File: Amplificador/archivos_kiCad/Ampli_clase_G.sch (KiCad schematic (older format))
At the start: 109 parts, among them J1 Conn_IN, J2 LOAD_CONN, J3 SUPPLY_CONN, Q1 BC856, Q10 BC846, Q11 2SC4793, Q14 2SC4793, Q15 2SA1837, Q16 2SC4793, Q17 2SA1837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

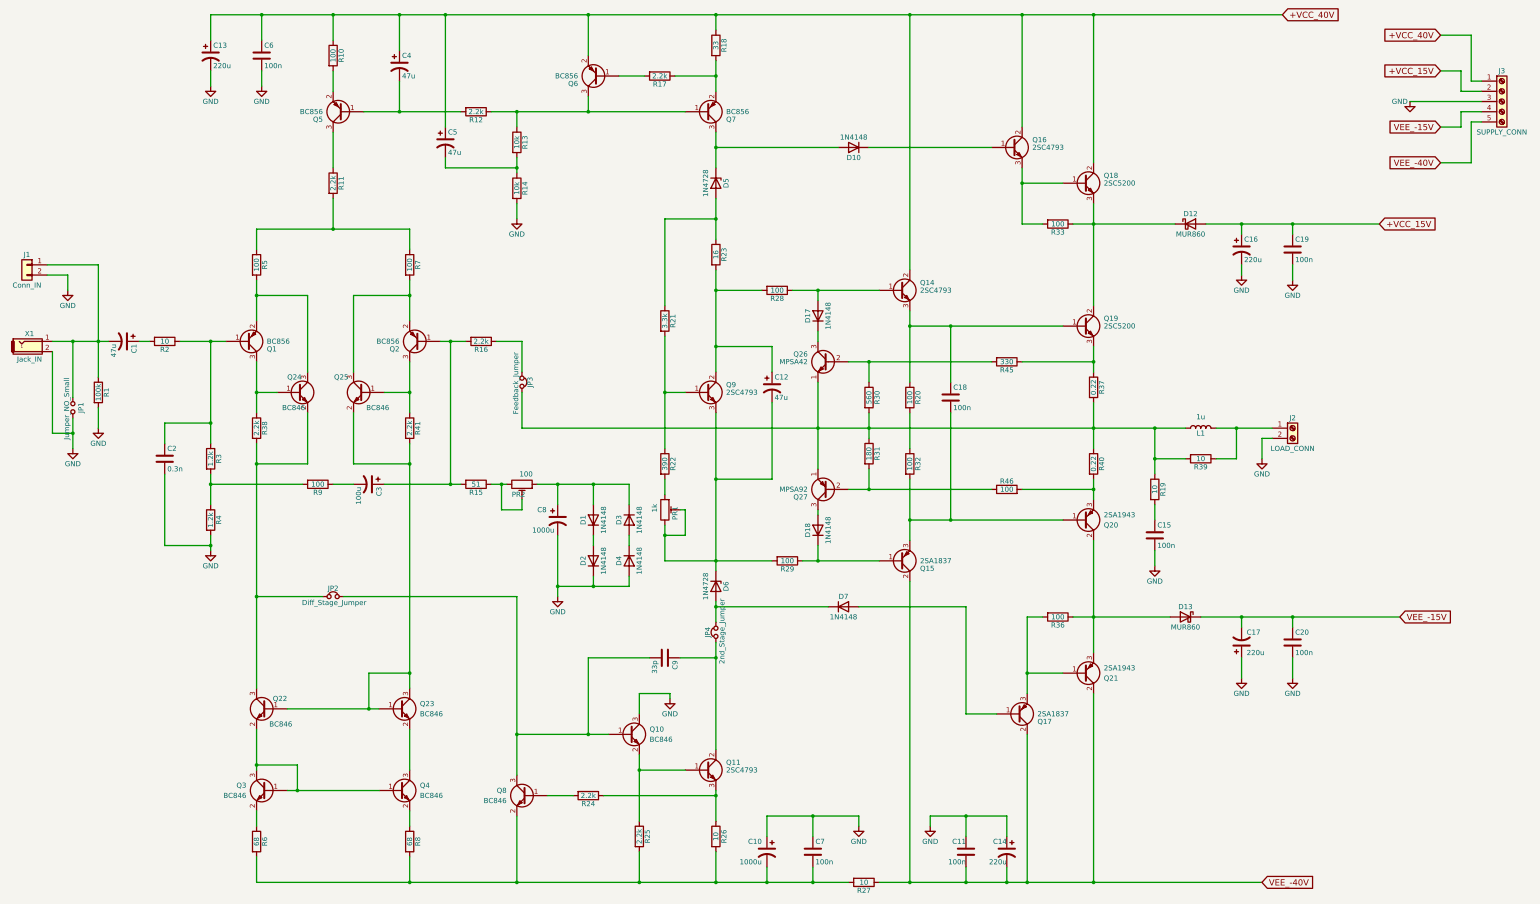
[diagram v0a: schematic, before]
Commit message: Cambios en el esquematico de Kicad- Jumpers
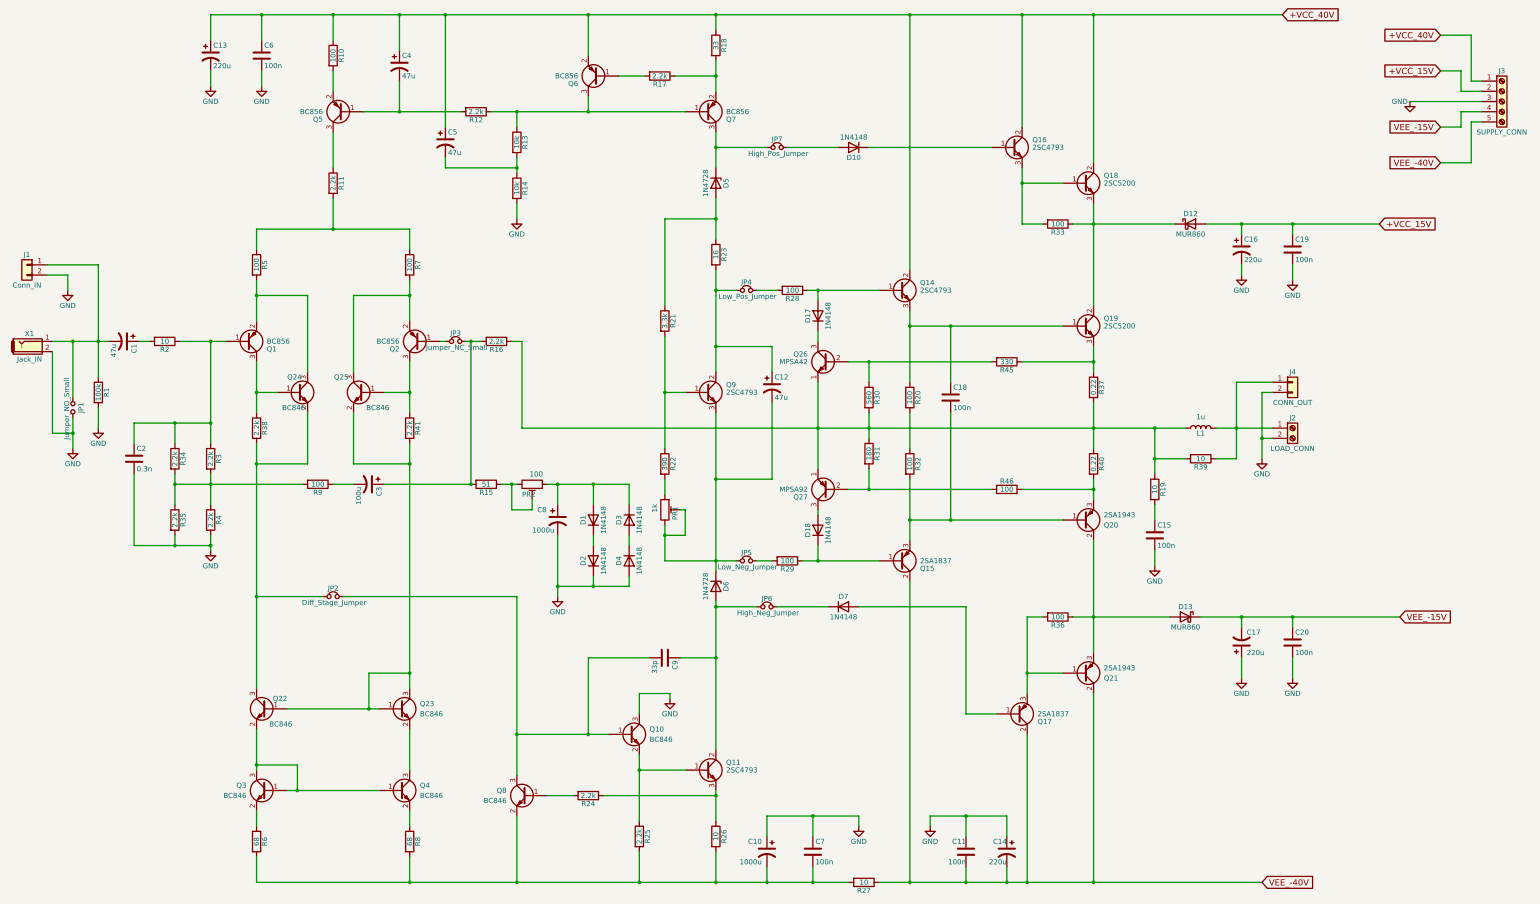
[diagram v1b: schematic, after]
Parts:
- added J4: CONN_OUT, Pin_Headers:Pin_Header_Straight_1x02_Pitch2.54mm, symbol Conn_01x02
- added JP5: Low_Neg_Jumper, Pin_Headers:Pin_Header_Straight_1x02_Pitch2.54mm, symbol Jumper_NC_Small
- added JP6: High_Neg_Jumper, Pin_Headers:Pin_Header_Straight_1x02_Pitch2.54mm, symbol Jumper_NC_Small
- added JP7: High_Pos_Jumper, Pin_Headers:Pin_Header_Straight_1x02_Pitch2.54mm, symbol Jumper_NC_Small
- added R34, R35: 2.2k, Resistors_SMD:R_0805_HandSoldering, symbol R
- JP3: value Feedback_Jumper -> Jumper_NC_Small
- JP4: value 2nd_Stage_Jumper -> Low_Pos_Jumper
- L1: footprint Inductors_THT:L_Axial_L5.3mm_D2.2mm_P10.16mm_Horizontal_Vishay_IM-1 -> Inductors_THT:L_Axial_L20.0mm_D8.0mm_P25.40mm_Horizontal
- R3, R4: value 1.2k -> 2.2k
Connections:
- net GND: now also J4.2 (Pin_2), R35.2
- net at C2.1, Q1.1 (B), R2.1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: now also R34.1
- net at C3.1, R15.2, R16.2: now also JP3.2; no longer Q2.1 (B)
- net at R3.2, R4.1, R9.2: now also R34.2, R35.1
- net at JP3.1: now also Q2.1 (B); no longer R16.1
- net at C9.1, Q11.2 (C): now also D6.2 (A), JP6.1; no longer JP4.1
- net at C12.2, D6.1 (K), PR1.2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: now also JP5.1; no longer R29.2
- net at C12.1, Q9.2 (C), R23.2: now also JP4.1; no longer R28.2
- net at D5.1 (K), Q7.3 (C): now also JP7.1; no longer D10.2 (A)
- net at J2.1 (Pin_1), L1.2, R39.1: now also J4.1 (Pin_1)
- net at L1.1, Q26.1 (E), Q27.1 (E)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: now also R16.1; no longer JP3.2
- new net: D10.2 (A), JP7.2
- new net: JP4.2, R28.2
- new net: D7.1 (K), JP6.2
- new net: JP5.2, R29.2
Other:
- moved on the sheet: C2, PR2, R15, R16, R28
